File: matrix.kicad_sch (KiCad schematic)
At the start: 203 parts

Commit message: sch fin
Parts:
- removed D? (x68): D, symbol Device:D
- removed S? (x133): MX1A, symbol MX1A:MX1A
- added D10, D11, D12, D13, D14, D15, D16, D17, D18, D19, D2, D20, D21, D22, D23, D24, D25, D26, D27, D28, D29, D3, D30, D31, D32, D33, D34, D35, D36, D37, D38, D39, D4, D40, D41, D42, D43, D44, D45, D46, D47, D48, D49, D5, D50, D51, D52, D53, D54, D55, D56, D57, D58, D59, D6, D60, D61, D62, D63, D64, D65, D66, D67, D68, D69, D7, D8, D9: D, Diode_SMD:D_0805_2012Metric_Pad1.15x1.40mm_HandSolder, symbol Device:D
- added S10, S11, S12, S13, S14, S15, S16, S17, S18, S19, S2, S20, S21, S22, S23, S24, S25, S26, S27, S28, S29, S3, S30, S31, S32, S33, S34, S35, S36, S37, S38, S39, S4, S40, S41, S42, S43, S44, S45, S46, S47, S48, S49, S5, S50, S51, S52, S53, S54, S55, S56, S57, S58, S59, S6, S60, S61, S62, S63, S64, S65, S66, S67, S68, S69, S7, S70, S71, S72, S73, S74, S75, S76, S77, S78, S79, S8, S80, S81, S82, S83, S9: MX1A, mx1a:KaiHua_Contact, symbol MX1A:MX1A
- D1: renamed from D?; footprint (none) -> Diode_SMD:D_0805_2012Metric_Pad1.15x1.40mm_HandSolder
- S1: renamed from S?; footprint (none) -> mx1a:KaiHua_Contact
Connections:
- net COL1: now also D2.2 (A), D3.2 (A), D4.2 (A), D5.2 (A)
- net COL10: now also D45.2 (A), D46.2 (A), D47.2 (A), D48.2 (A), D49.2 (A)
- net COL11: now also D50.2 (A), D51.2 (A), D52.2 (A), D53.2 (A), D54.2 (A)
- net COL12: now also D55.2 (A), D56.2 (A), D57.2 (A), D58.2 (A), D59.2 (A)
- net COL13: now also D60.2 (A), D61.2 (A), D62.2 (A), D63.2 (A), D64.2 (A)
- net COL14: now also D65.2 (A), D66.2 (A), D67.2 (A), D68.2 (A), D69.2 (A)
- net COL2: now also D10.2 (A), D6.2 (A), D7.2 (A), D8.2 (A), D9.2 (A)
- net COL3: now also D11.2 (A), D12.2 (A), D13.2 (A), D14.2 (A), D15.2 (A)
- net COL4: now also D16.2 (A), D17.2 (A), D18.2 (A), D19.2 (A), D20.2 (A)
- net COL5: now also D21.2 (A), D22.2 (A), D23.2 (A), D24.2 (A)
- net COL6: now also D25.2 (A), D26.2 (A), D27.2 (A), D28.2 (A), D29.2 (A)
- net COL7: now also D30.2 (A), D31.2 (A), D32.2 (A), D33.2 (A), D34.2 (A)
- net COL8: now also D35.2 (A), D36.2 (A), D37.2 (A), D38.2 (A), D39.2 (A)
- net COL9: now also D40.2 (A), D41.2 (A), D42.2 (A), D43.2 (A), D44.2 (A)
- net ROW1: now also S14.2, S19.2, S25.2, S29.2, S34.2, S39.2, S44.2, S49.2, S54.2, S60.2, S66.2, S7.2, S74.2, S75.2
- net ROW2: now also S15.2, S2.2, S20.2, S26.2, S30.2, S35.2, S40.2, S45.2, S50.2, S55.2, S61.2, S67.2, S76.2, S77.2, S8.2
- net ROW3: now also S16.2, S21.2, S27.2, S3.2, S31.2, S36.2, S41.2, S46.2, S51.2, S56.2, S62.2, S68.2, S78.2, S79.2, S80.2, S9.2
- net ROW4: now also S10.2, S11.2, S12.2, S17.2, S22.2, S28.2, S32.2, S37.2, S4.2, S42.2, S47.2, S5.2, S52.2, S57.2, S63.2, S69.2, S70.2, S71.2, S81.2, S82.2
- net ROW5: now also S13.2, S18.2, S23.2, S24.2, S33.2, S38.2, S43.2, S48.2, S53.2, S58.2, S59.2, S6.2, S64.2, S65.2, S72.2, S73.2, S83.2
- new net: D32.1 (K), S36.1
- new net: D45.1 (K), S49.1
- new net: D10.1 (K), S13.1
- new net: D59.1 (K), S64.1, S65.1
- new net: D31.1 (K), S35.1
- new net: D43.1 (K), S47.1
- new net: D9.1 (K), S10.1, S11.1, S12.1
- new net: D36.1 (K), S40.1
- new net: D29.1 (K), S33.1
- new net: D39.1 (K), S43.1
- new net: D3.1 (K), S3.1
- new net: D37.1 (K), S41.1
- new net: D20.1 (K), S23.1, S24.1
- new net: D67.1 (K), S78.1, S79.1, S80.1
- new net: D38.1 (K), S42.1
- new net: D12.1 (K), S15.1
- new net: D61.1 (K), S67.1
- new net: D21.1 (K), S25.1
- new net: D54.1 (K), S58.1, S59.1
- new net: D48.1 (K), S52.1
- new net: D57.1 (K), S62.1
- new net: D8.1 (K), S9.1
- new net: D7.1 (K), S8.1
- new net: D63.1 (K), S69.1, S70.1, S71.1
- new net: D6.1 (K), S7.1
- new net: D55.1 (K), S60.1
- new net: D46.1 (K), S50.1
- new net: D23.1 (K), S27.1
- new net: D50.1 (K), S54.1
- new net: D69.1 (K), S83.1
- new net: D62.1 (K), S68.1
- new net: D16.1 (K), S19.1
- new net: D51.1 (K), S55.1
- new net: D11.1 (K), S14.1
- new net: D65.1 (K), S74.1, S75.1
- new net: D2.1 (K), S2.1
- new net: D25.1 (K), S29.1
- new net: D64.1 (K), S72.1, S73.1
- new net: D66.1 (K), S76.1, S77.1
- new net: D4.1 (K), S4.1, S5.1
- new net: D24.1 (K), S28.1
- new net: D13.1 (K), S16.1
- new net: D42.1 (K), S46.1
- new net: D68.1 (K), S81.1, S82.1
- new net: D58.1 (K), S63.1
- new net: D18.1 (K), S21.1
- new net: D52.1 (K), S56.1
- new net: D49.1 (K), S53.1
- new net: D15.1 (K), S18.1
- new net: D33.1 (K), S37.1
- new net: D56.1 (K), S61.1
- new net: D27.1 (K), S31.1
- new net: D5.1 (K), S6.1
- new net: D60.1 (K), S66.1
- new net: D17.1 (K), S20.1
- new net: D30.1 (K), S34.1
- new net: D28.1 (K), S32.1
- new net: D19.1 (K), S22.1
- new net: D35.1 (K), S39.1
- new net: D26.1 (K), S30.1
- new net: D53.1 (K), S57.1
- new net: D14.1 (K), S17.1
- new net: D34.1 (K), S38.1
- new net: D41.1 (K), S45.1
- new net: D22.1 (K), S26.1
- new net: D40.1 (K), S44.1
- new net: D44.1 (K), S48.1
- new net: D47.1 (K), S51.1

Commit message: 20220326 pcb init
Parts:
- removed S77: MX1A, mx1a:KaiHua_Contact, symbol MX1A:MX1A
- S1, S10, S14, S15, S16, S17, S19, S20, S21, S22, S25, S26, S27, S28, S29, S30, S31, S32, S33, S34, S35, S36, S37, S38, S39, S40, S41, S42, S43, S44, S45, S46, S47, S48, S49, S5, S50, S51, S52, S53, S54, S55, S56, S57, S58, S60, S61, S62, S63, S64, S66, S67, S68, S7, S72, S74, S8, S9: footprint mx1a:KaiHua_Contact -> mx1a:KaiHua_Contact_1.00u
- S11, S13, S18, S4, S59, S6, S65, S69, S73: footprint mx1a:KaiHua_Contact -> mx1a:KaiHua_Contact_1.25u
- S12: footprint mx1a:KaiHua_Contact -> mx1a:KaiHua_Contact_2.25u
- S2, S76: footprint mx1a:KaiHua_Contact -> mx1a:KaiHua_Contact_1.50u
- S23: footprint mx1a:KaiHua_Contact -> mx1a:KaiHua_Contact_3.00u
- S24: footprint mx1a:KaiHua_Contact -> mx1a:KaiHua_Contact_6.25u
- S3, S70: footprint mx1a:KaiHua_Contact -> mx1a:KaiHua_Contact_1.75u
- S71: footprint mx1a:KaiHua_Contact -> mx1a:KaiHua_Contact_2.75u
- S75: footprint mx1a:KaiHua_Contact -> mx1a:KaiHua_Contact_2.00u
- S77: renamed from S78; footprint mx1a:KaiHua_Contact -> mx1a:KaiHua_Contact_1.25u
- S78: renamed from S79; footprint mx1a:KaiHua_Contact -> mx1a:KaiHua_Contact_ISO_Enter
- S79: renamed from S80; footprint mx1a:KaiHua_Contact -> mx1a:KaiHua_Contact_2.25u
- S80: renamed from S81; footprint mx1a:KaiHua_Contact -> mx1a:KaiHua_Contact_1.00u
- S81: renamed from S82; footprint mx1a:KaiHua_Contact -> mx1a:KaiHua_Contact_1.75u
- S82: renamed from S83; footprint mx1a:KaiHua_Contact -> mx1a:KaiHua_Contact_1.25u
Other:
- moved on the sheet: D66

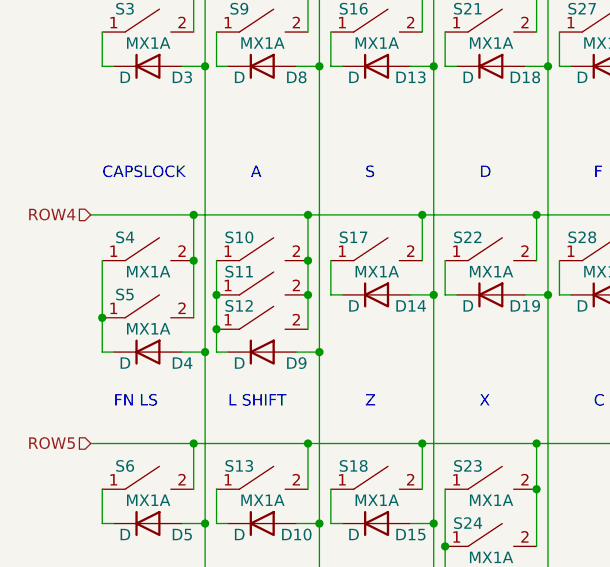
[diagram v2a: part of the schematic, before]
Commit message: 20220326 pcb: keycap mount
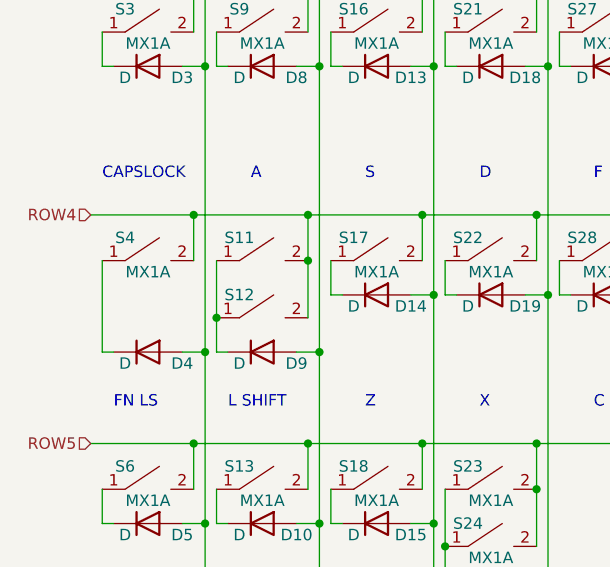
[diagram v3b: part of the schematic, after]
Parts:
- removed S10, S5: MX1A, mx1a:KaiHua_Contact_1.00u, symbol MX1A:MX1A
- S4, S69: footprint mx1a:KaiHua_Contact_1.25u -> mx1a:KaiHua_Contact_1.00u
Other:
- moved on the sheet: S11, S12
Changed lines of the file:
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@@
   (junction (at 101.6 154.94) (diameter 0) (color 0 0 0 0)
   )
-  (junction (at 62.23 119.38) (diameter 0) (color 0 0 0 0)
-  )
   (junction (at 201.93 114.3) (diameter 0) (color 0 0 0 0)
   )
@@
   (junction (at 176.53 139.7) (diameter 0) (color 0 0 0 0)
   )
-  (junction (at 74.93 119.38) (diameter 0) (color 0 0 0 0)
-  )
   (junction (at 201.93 144.78) (diameter 0) (color 0 0 0 0)
   )
@@
   (junction (at 100.33 63.5) (diameter 0) (color 0 0 0 0)
   )
-  (junction (at 52.07 125.73) (diameter 0) (color 0 0 0 0)
-  )
   (junction (at 152.4 123.19) (diameter 0) (color 0 0 0 0)
   )
@@
   (junction (at 100.33 38.1) (diameter 0) (color 0 0 0 0)
   )
-  (junction (at 64.77 123.19) (diameter 0) (color 0 0 0 0)
-  )
   (junction (at 214.63 123.19) (diameter 0) (color 0 0 0 0)
   )
+  (junction (at 64.77 125.73) (diameter 0) (color 0 0 0 0)
+  )
   (junction (at 228.6 72.39) (diameter 0) (color 0 0 0 0)
   )
@@
   (junction (at 201.93 63.5) (diameter 0) (color 0 0 0 0)
   )
-  (junction (at 74.93 123.19) (diameter 0) (color 0 0 0 0)
-  )
   (junction (at 139.7 46.99) (diameter 0) (color 0 0 0 0)
   )
@@
   (junction (at 165.1 123.19) (diameter 0) (color 0 0 0 0)
   )
+  (junction (at 74.93 119.38) (diameter 0) (color 0 0 0 0)
+  )
   (junction (at 76.2 72.39) (diameter 0) (color 0 0 0 0)
   )
@@
   (junction (at 74.93 88.9) (diameter 0) (color 0 0 0 0)
   )
-  (junction (at 64.77 127) (diameter 0) (color 0 0 0 0)
-  )
   (junction (at 189.23 63.5) (diameter 0) (color 0 0 0 0)
   )
@@
     (stroke (width 0) (type default) (color 0 0 0 0))
   )
+  (wire (pts (xy 64.77 125.73) (xy 64.77 129.54))
+    (stroke (width 0) (type default) (color 0 0 0 0))
+  )
   (wire (pts (xy 101.6 72.39) (xy 101.6 97.79))
     (stroke (width 0) (type default) (color 0 0 0 0))
@@
     (stroke (width 0) (type default) (color 0 0 0 0))
   )
-  (wire (pts (xy 64.77 123.19) (xy 64.77 127))
-    (stroke (width 0) (type default) (color 0 0 0 0))
-  )
   (wire (pts (xy 153.67 144.78) (xy 153.67 148.59))
     (stroke (width 0) (type default) (color 0 0 0 0))
@@
     (stroke (width 0) (type default) (color 0 0 0 0))
   )
-  (wire (pts (xy 74.93 119.38) (xy 74.93 114.3))
+  (wire (pts (xy 74.93 114.3) (xy 74.93 119.38))
     (stroke (width 0) (type default) (color 0 0 0 0))
   )
@@
     (stroke (width 0) (type default) (color 0 0 0 0))
   )
+  (wire (pts (xy 74.93 119.38) (xy 74.93 125.73))
+    (stroke (width 0) (type default) (color 0 0 0 0))
+  )
   (wire (pts (xy 217.17 93.98) (xy 217.17 97.79))
     (stroke (width 0) (type default) (color 0 0 0 0))
@@
     (stroke (width 0) (type default) (color 0 0 0 0))
   )
-  (wire (pts (xy 52.07 119.38) (xy 52.07 125.73))
-    (stroke (width 0) (type default) (color 0 0 0 0))
-  )
   (wire (pts (xy 204.47 68.58) (xy 204.47 72.39))
     (stroke (width 0) (type default) (color 0 0 0 0))
@@
     (stroke (width 0) (type default) (color 0 0 0 0))
   )
-  (wire (pts (xy 74.93 123.19) (xy 74.93 127))
-    (stroke (width 0) (type default) (color 0 0 0 0))
-  )
   (wire (pts (xy 62.23 63.5) (xy 74.93 63.5))
     (stroke (width 0) (type default) (color 0 0 0 0))
@@
     (stroke (width 0) (type default) (color 0 0 0 0))
   )
-  (wire (pts (xy 74.93 119.38) (xy 74.93 123.19))
-    (stroke (width 0) (type default) (color 0 0 0 0))
-  )
   (wire (pts (xy 152.4 97.79) (xy 152.4 123.19))
     (stroke (width 0) (type default) (color 0 0 0 0))
@@
     (stroke (width 0) (type default) (color 0 0 0 0))
   )
-  (wire (pts (xy 64.77 127) (xy 64.77 129.54))
-    (stroke (width 0) (type default) (color 0 0 0 0))
-  )
   (wire (pts (xy 214.63 119.38) (xy 214.63 123.19))
     (stroke (width 0) (type default) (color 0 0 0 0))
@@
     (stroke (width 0) (type default) (color 0 0 0 0))
   )
-  (wire (pts (xy 62.23 119.38) (xy 62.23 125.73))
-    (stroke (width 0) (type default) (color 0 0 0 0))
-  )
   (wire (pts (xy 102.87 46.99) (xy 104.14 46.99))
     (stroke (width 0) (type default) (color 0 0 0 0))
@@
     (stroke (width 0) (type default) (color 0 0 0 0))
   )
-  (wire (pts (xy 52.07 125.73) (xy 52.07 129.54))
+  (wire (pts (xy 52.07 119.38) (xy 52.07 129.54))
     (stroke (width 0) (type default) (color 0 0 0 0))
   )
@@
     (stroke (width 0) (type default) (color 0 0 0 0))
   )
-  (wire (pts (xy 64.77 119.38) (xy 64.77 123.19))
+  (wire (pts (xy 64.77 119.38) (xy 64.77 125.73))
     (stroke (width 0) (type default) (color 0 0 0 0))
   )
@@
     (pin "2")
   )
-  (symbol (lib_id "MX1A:MX1A") (at 69.85 119.38 0) (unit 1)
-    (in_bom yes) (on_board yes)
-    (property "Reference" "S10" (id 0) (at 67.31 116.84 0))
-    (property "Value" "MX1A" (id 1) (at 69.85 120.65 0)
-      (effects (font (size 1.27 1.27)) hide)
-    )
-    (property "Footprint" "mx1a:KaiHua_Contact_1.00u" (id 2) (at 83.82 127 0)
-      (effects (font (size 1.27 1.27)) hide)
-    )
-    (property "Datasheet" "" (id 3) (at 83.82 127 0)
-      (effects (font (size 1.27 1.27)) hide)
-    )
-    (pin "1")
-    (pin "2")
-  )
   (symbol (lib_id "MX1A:MX1A") (at 209.55 151.13 0) (unit 1)
     (in_bom yes) (on_board yes)
@@
     (pin "2")
   )
-  (symbol (lib_id "MX1A:MX1A") (at 57.15 125.73 0) (unit 1)
-    (in_bom yes) (on_board yes)
-    (property "Reference" "S5" (id 0) (at 54.61 123.19 0))
-    (property "Value" "MX1A" (id 1) (at 57.15 127 0))
-    (property "Footprint" "mx1a:KaiHua_Contact_1.00u" (id 2) (at 71.12 133.35 0)
-      (effects (font (size 1.27 1.27)) hide)
-    )
-    (property "Datasheet" "" (id 3) (at 71.12 133.35 0)
-      (effects (font (size 1.27 1.27)) hide)
-    )
-    (pin "1")
-    (pin "2")
-  )
   (symbol (lib_id "MX1A:MX1A") (at 171.45 43.18 0) (unit 1)
     (in_bom yes) (on_board yes)
@@
       (effects (font (size 1.27 1.27)) hide)
     )
-    (property "Footprint" "mx1a:KaiHua_Contact_1.25u" (id 2) (at 223.52 127 0)
+    (property "Footprint" "mx1a:KaiHua_Contact_1.00u" (id 2) (at 223.52 127 0)
       (effects (font (size 1.27 1.27)) hide)
     )
@@
     (pin "2")
   )
-  (symbol (lib_id "MX1A:MX1A") (at 69.85 123.19 0) (unit 1)
+  (symbol (lib_id "MX1A:MX1A") (at 69.85 119.38 0) (unit 1)
     (in_bom yes) (on_board yes)
-    (property "Reference" "S11" (id 0) (at 67.31 120.65 0))
-    (property "Value" "MX1A" (id 1) (at 69.85 124.46 0)
+    (property "Reference" "S11" (id 0) (at 67.31 116.84 0))
+    (property "Value" "MX1A" (id 1) (at 69.85 120.65 0)
       (effects (font (size 1.27 1.27)) hide)
     )
-    (property "Footprint" "mx1a:KaiHua_Contact_1.25u" (id 2) (at 83.82 130.81 0)
+    (property "Footprint" "mx1a:KaiHua_Contact_1.25u" (id 2) (at 83.82 127 0)
       (effects (font (size 1.27 1.27)) hide)
     )
-    (property "Datasheet" "" (id 3) (at 83.82 130.81 0)
+    (property "Datasheet" "" (id 3) (at 83.82 127 0)
       (effects (font (size 1.27 1.27)) hide)
     )
@@
     (property "Reference" "S4" (id 0) (at 54.61 116.84 0))
     (property "Value" "MX1A" (id 1) (at 57.15 120.65 0))
-    (property "Footprint" "mx1a:KaiHua_Contact_1.25u" (id 2) (at 71.12 127 0)
+    (property "Footprint" "mx1a:KaiHua_Contact_1.00u" (id 2) (at 71.12 127 0)
       (effects (font (size 1.27 1.27)) hide)
     )
@@
     (pin "2")
   )
-  (symbol (lib_id "MX1A:MX1A") (at 69.85 127 0) (unit 1)
+  (symbol (lib_id "MX1A:MX1A") (at 69.85 125.73 0) (unit 1)
     (in_bom yes) (on_board yes)
-    (property "Reference" "S12" (id 0) (at 67.31 124.46 0))
-    (property "Value" "MX1A" (id 1) (at 69.85 128.27 0)
+    (property "Reference" "S12" (id 0) (at 67.31 123.19 0))
+    (property "Value" "MX1A" (id 1) (at 69.85 127 0)
       (effects (font (size 1.27 1.27)) hide)
     )
-    (property "Footprint" "mx1a:KaiHua_Contact_2.25u" (id 2) (at 83.82 134.62 0)
+    (property "Footprint" "mx1a:KaiHua_Contact_2.25u" (id 2) (at 83.82 133.35 0)
       (effects (font (size 1.27 1.27)) hide)
     )
-    (property "Datasheet" "" (id 3) (at 83.82 134.62 0)
+    (property "Datasheet" "" (id 3) (at 83.82 133.35 0)
       (effects (font (size 1.27 1.27)) hide)
     )

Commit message: 20220326 fin
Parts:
- removed S78: MX1A, mx1a:KaiHua_Contact_ISO_Enter, symbol MX1A:MX1A
- S75: footprint mx1a:KaiHua_Contact_2.00u -> mx1a:KaiHua_Contact_2.00u_reverse
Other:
- moved on the sheet: S79
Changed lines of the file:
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@@
   (junction (at 191.77 151.13) (diameter 0) (color 0 0 0 0)
   )
-  (junction (at 217.17 101.6) (diameter 0) (color 0 0 0 0)
-  )
   (junction (at 165.1 148.59) (diameter 0) (color 0 0 0 0)
   )
@@
   (junction (at 203.2 97.79) (diameter 0) (color 0 0 0 0)
   )
-  (junction (at 217.17 97.79) (diameter 0) (color 0 0 0 0)
-  )
   (junction (at 176.53 114.3) (diameter 0) (color 0 0 0 0)
   )
@@
   (junction (at 227.33 93.98) (diameter 0) (color 0 0 0 0)
   )
+  (junction (at 217.17 100.33) (diameter 0) (color 0 0 0 0)
+  )
   (junction (at 215.9 72.39) (diameter 0) (color 0 0 0 0)
   )
@@
   (junction (at 63.5 46.99) (diameter 0) (color 0 0 0 0)
   )
-  (junction (at 227.33 97.79) (diameter 0) (color 0 0 0 0)
-  )
   (junction (at 138.43 38.1) (diameter 0) (color 0 0 0 0)
   )
@@
     (stroke (width 0) (type default) (color 0 0 0 0))
   )
-  (wire (pts (xy 227.33 97.79) (xy 227.33 101.6))
-    (stroke (width 0) (type default) (color 0 0 0 0))
-  )
   (wire (pts (xy 64.77 125.73) (xy 64.77 129.54))
     (stroke (width 0) (type default) (color 0 0 0 0))
@@
     (stroke (width 0) (type default) (color 0 0 0 0))
   )
-  (wire (pts (xy 227.33 93.98) (xy 227.33 97.79))
+  (wire (pts (xy 227.33 93.98) (xy 227.33 100.33))
     (stroke (width 0) (type default) (color 0 0 0 0))
   )
@@
     (stroke (width 0) (type default) (color 0 0 0 0))
   )
-  (wire (pts (xy 217.17 93.98) (xy 217.17 97.79))
+  (wire (pts (xy 217.17 93.98) (xy 217.17 100.33))
     (stroke (width 0) (type default) (color 0 0 0 0))
   )
@@
     (stroke (width 0) (type default) (color 0 0 0 0))
   )
-  (wire (pts (xy 217.17 101.6) (xy 217.17 104.14))
-    (stroke (width 0) (type default) (color 0 0 0 0))
-  )
   (wire (pts (xy 76.2 148.59) (xy 76.2 165.1))
     (stroke (width 0) (type default) (color 0 0 0 0))
@@
     (stroke (width 0) (type default) (color 0 0 0 0))
   )
+  (wire (pts (xy 217.17 100.33) (xy 217.17 104.14))
+    (stroke (width 0) (type default) (color 0 0 0 0))
+  )
   (wire (pts (xy 115.57 72.39) (xy 116.84 72.39))
     (stroke (width 0) (type default) (color 0 0 0 0))
@@
     (stroke (width 0) (type default) (color 0 0 0 0))
   )
-  (wire (pts (xy 217.17 97.79) (xy 217.17 101.6))
-    (stroke (width 0) (type default) (color 0 0 0 0))
-  )
   (wire (pts (xy 166.37 123.19) (xy 167.64 123.19))
     (stroke (width 0) (type default) (color 0 0 0 0))
@@
     (pin "2")
   )
-  (symbol (lib_id "MX1A:MX1A") (at 222.25 97.79 0) (unit 1)
-    (in_bom yes) (on_board yes)
-    (property "Reference" "S78" (id 0) (at 219.71 95.25 0))
-    (property "Value" "MX1A" (id 1) (at 222.25 99.06 0)
-      (effects (font (size 1.27 1.27)) hide)
-    )
-    (property "Footprint" "mx1a:KaiHua_Contact_ISO_Enter" (id 2) (at 236.22 105.41 0)
-      (effects (font (size 1.27 1.27)) hide)
-    )
-    (property "Datasheet" "" (id 3) (at 236.22 105.41 0)
-      (effects (font (size 1.27 1.27)) hide)
-    )
-    (pin "1")
-    (pin "2")
-  )
   (symbol (lib_id "MX1A:MX1A") (at 146.05 119.38 0) (unit 1)
     (in_bom yes) (on_board yes)
@@
     (property "Reference" "S75" (id 0) (at 219.71 46.99 0))
     (property "Value" "MX1A" (id 1) (at 222.25 50.8 0))
-    (property "Footprint" "mx1a:KaiHua_Contact_2.00u" (id 2) (at 236.22 57.15 0)
+    (property "Footprint" "mx1a:KaiHua_Contact_2.00u_reverse" (id 2) (at 236.22 57.15 0)
       (effects (font (size 1.27 1.27)) hide)
     )
@@
     (pin "2")
   )
-  (symbol (lib_id "MX1A:MX1A") (at 222.25 101.6 0) (unit 1)
+  (symbol (lib_id "MX1A:MX1A") (at 222.25 100.33 0) (unit 1)
     (in_bom yes) (on_board yes)
-    (property "Reference" "S79" (id 0) (at 219.71 99.06 0))
-    (property "Value" "MX1A" (id 1) (at 222.25 102.87 0)
+    (property "Reference" "S79" (id 0) (at 219.71 97.79 0))
+    (property "Value" "MX1A" (id 1) (at 222.25 101.6 0)
       (effects (font (size 1.27 1.27)) hide)
     )
-    (property "Footprint" "mx1a:KaiHua_Contact_2.25u" (id 2) (at 236.22 109.22 0)
+    (property "Footprint" "mx1a:KaiHua_Contact_2.25u" (id 2) (at 236.22 107.95 0)
       (effects (font (size 1.27 1.27)) hide)
     )
-    (property "Datasheet" "" (id 3) (at 236.22 109.22 0)
+    (property "Datasheet" "" (id 3) (at 236.22 107.95 0)
       (effects (font (size 1.27 1.27)) hide)
     )
